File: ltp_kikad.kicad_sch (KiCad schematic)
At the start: 27 parts, among them J2 RPi_GPIO, J3 SM04B-SRSS-TB(LF)(SN)

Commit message: Version 0.05
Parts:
- removed C6 (x2): 4.7uF, Capacitor_SMD:C_0603_1608Metric, symbol Device:C_Small
- removed C7 (x2): 0.1uF, Capacitor_SMD:C_0603_1608Metric, symbol Device:C_Small
- removed J3: SM04B-SRSS-TB(LF)(SN), LTP-305G:JST_SM04B-SRSS-TB(LF)(SN), symbol SM04B-SRSS-TB_LF__SN_:SM04B-SRSS-TB(LF)(SN)
- removed R3 (x2), R5 (x2): DNP, Resistor_SMD:R_0603_1608Metric_Pad0.98x0.95mm_HandSolder, symbol Device:R
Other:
- added sheet Qwiik stemma connector (i2c_connector.kicad_sch)
- note removed: "I2C1_SCL"
- note removed: "I2C1_SDA"
- note removed: "Qwiic/Stemma"
- moved on the sheet: C11

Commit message: Version 0.06
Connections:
- net GND: now also J2.14 (GND), J2.20 (GND), J2.25 (GND), J2.30 (GND), J2.34 (GND), J2.9 (GND)
- no-connect marks 6 -> 5
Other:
- moved on the sheet: C11

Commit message: Add rp2040 mcu, remove mcp2515
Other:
- removed sheet CAN Transiver
- added sheet MCU (mcu.kicad_sch)
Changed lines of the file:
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@@
     (instances
       (project "ltp_kikad"
-        (path "/eed35b77-cbf9-4596-9b17-2558f81058ba/d18f2354-5f56-48bf-919b-3fdf8c87b820"
-          (reference "#PWR045") (unit 1)
-        )
         (path "/eed35b77-cbf9-4596-9b17-2558f81058ba"
           (reference "#PWR058") (unit 1)
@@
     (instances
       (project "ltp_kikad"
-        (path "/eed35b77-cbf9-4596-9b17-2558f81058ba/d18f2354-5f56-48bf-919b-3fdf8c87b820"
-          (reference "#PWR045") (unit 1)
-        )
         (path "/eed35b77-cbf9-4596-9b17-2558f81058ba"
           (reference "#PWR059") (unit 1)
@@
     )
   )
+  (sheet (at 116.84 33.02) (size 57.15 7.62) (fields_autoplaced)
+    (stroke (width 0.1524) (type solid))
+    (fill (color 0 0 0 0.0000))
+    (property "Sheetname" "MCU" (at 116.84 32.3084 0)
+      (effects (font (size 1.27 1.27)) (justify left bottom))
+    )
+    (property "Sheetfile" "mcu.kicad_sch" (at 116.84 41.2246 0)
+      (effects (font (size 1.27 1.27)) (justify left top))
+    )
+    (instances
+      (project "ltp_kikad"
+        (path "/eed35b77-cbf9-4596-9b17-2558f81058ba" (page "6"))
+      )
+    )
+  )
   (sheet (at 116.84 59.69) (size 57.15 7.62) (fields_autoplaced)
     (stroke (width 0.1524) (type solid))
@@
       )
     )
-  )
-  (sheet (at 116.84 45.72) (size 57.15 7.62) (fields_autoplaced)
-    (stroke (width 0.1524) (type solid))
-    (fill (color 0 0 0 0.0000))
-    (property "Sheetname" "CAN Transiver" (at 116.84 45.0084 0)
-      (effects (font (size 1.27 1.27)) (justify left bottom))
-    )
-    (property "Sheetfile" "mdlh_can_ransiver.kicad_sch" (at 116.84 53.9246 0)
-      (effects (font (size 1.27 1.27)) (justify left top))
-    )
-    (instances
-      (project "ltp_kikad"
-        (path "/eed35b77-cbf9-4596-9b17-2558f81058ba" (page "2"))
-      )
-    )

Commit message: Add mcp 2517 can transceiver
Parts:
- removed C11: 10uF, Capacitor_SMD:C_0603_1608Metric, symbol Device:C_Small
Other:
- added sheet CAN (can.kicad_sch)
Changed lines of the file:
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@@
-    (stroke (width 0) (type default))
-  )
-  (wire (pts (xy 242.57 101.6) (xy 242.57 109.22))
     (stroke (width 0) (type default))
   )
@@
         (path "/eed35b77-cbf9-4596-9b17-2558f81058ba"
           (reference "#PWR013") (unit 1)
-        )
-      )
-    )
-  )
-  (symbol (lib_id "power:GND") (at 242.57 114.3 0) (unit 1)
-    (in_bom yes) (on_board yes) (dnp no)
-    (property "Reference" "#PWR038" (at 242.57 120.65 0)
-      (effects (font (size 1.27 1.27)) hide)
-    )
-    (property "Value" "GND" (at 242.697 118.6942 0)
-      (effects (font (size 1.27 1.27)))
-    )
-    (property "Footprint" "" (at 242.57 114.3 0)
-      (effects (font (size 1.27 1.27)) hide)
-    )
-    (property "Datasheet" "" (at 242.57 114.3 0)
-      (effects (font (size 1.27 1.27)) hide)
-    )
-    (pin "1")
-    (instances
-      (project "LTP305_ESP32_CLOCK"
-        (path "/c007e288-8439-49d9-bbdf-49724c34958c"
-          (reference "#PWR038") (unit 1)
-        )
-      )
-      (project "ltp_kikad"
-        (path "/eed35b77-cbf9-4596-9b17-2558f81058ba"
-          (reference "#PWR034") (unit 1)
         )
       )
@@
     )
   )
-  (symbol (lib_id "power:+5V") (at 242.57 101.6 270) (unit 1)
-    (in_bom yes) (on_board yes) (dnp no)
-    (property "Reference" "#PWR08" (at 238.76 101.6 0)
-      (effects (font (size 1.27 1.27)) hide)
-    )
-    (property "Value" "+5V" (at 246.9642 101.981 0)
-      (effects (font (size 1.27 1.27)))
-    )
-    (property "Footprint" "" (at 242.57 101.6 0)
-      (effects (font (size 1.27 1.27)) hide)
-    )
-    (property "Datasheet" "" (at 242.57 101.6 0)
-      (effects (font (size 1.27 1.27)) hide)
-    )
-    (pin "1")
-    (instances
-      (project "LTP305_ESP32_CLOCK"
-        (path "/c007e288-8439-49d9-bbdf-49724c34958c"
-          (reference "#PWR08") (unit 1)
-        )
-      )
-      (project "ltp_kikad"
-        (path "/eed35b77-cbf9-4596-9b17-2558f81058ba"
-          (reference "#PWR033") (unit 1)
-        )
-      )
-    )
-  )
   (symbol (lib_id "LTP-305G:LTP-305G") (at 30.48 92.71 0) (unit 1)
     (in_bom yes) (on_board yes) (dnp no) (fields_autoplaced)
@@
     )
   )
-  (symbol (lib_id "Device:C_Small") (at 242.57 111.76 0) (unit 1)
-    (in_bom yes) (on_board yes) (dnp no)
-    (property "Reference" "C11" (at 244.9068 110.5916 0)
-      (effects (font (size 1.27 1.27)) (justify left))
-    )
-    (property "Value" "10uF" (at 237.49 114.3 0)
-      (effects (font (size 1.27 1.27)) (justify left))
-    )
-    (property "Footprint" "Capacitor_SMD:C_0603_1608Metric" (at 242.57 111.76 0)
-      (effects (font (size 1.27 1.27)) hide)
-    )
-    (property "Datasheet" "~" (at 242.57 111.76 0)
-      (effects (font (size 1.27 1.27)) hide)
-    )
-    (pin "1")
-    (pin "2")
-    (instances
-      (project "LTP305_ESP32_CLOCK"
-        (path "/c007e288-8439-49d9-bbdf-49724c34958c"
-          (reference "C11") (unit 1)
-        )
-      )
-      (project "ltp_kikad"
-        (path "/eed35b77-cbf9-4596-9b17-2558f81058ba"
-          (reference "C17") (unit 1)
-        )
-      )
-    )
-  )
   (symbol (lib_id "Device:C_Small") (at 163.83 114.3 0) (unit 1)
     (in_bom yes) (on_board yes) (dnp no)
@@
           (reference "#PWR025") (unit 1)
         )
+      )
+    )
+  )
+  (sheet (at 116.84 20.32) (size 57.15 6.35) (fields_autoplaced)
+    (stroke (width 0.1524) (type solid))
+    (fill (color 0 0 0 0.0000))
+    (property "Sheetname" "CAN" (at 116.84 19.6084 0)
+      (effects (font (size 1.27 1.27)) (justify left bottom))
+    )
+    (property "Sheetfile" "can.kicad_sch" (at 116.84 27.2546 0)
+      (effects (font (size 1.27 1.27)) (justify left top))
+    )
+    (instances
+      (project "ltp_kikad"
+        (path "/eed35b77-cbf9-4596-9b17-2558f81058ba" (page "6"))
       )
     )
@@
     (instances
       (project "ltp_kikad"
-        (path "/eed35b77-cbf9-4596-9b17-2558f81058ba" (page "6"))
-      )
-    )
+        (path "/eed35b77-cbf9-4596-9b17-2558f81058ba" (page "7"))
+      )
+    )

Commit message: Verssion 0.11
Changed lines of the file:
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@@
   (junction (at 267.97 41.91) (diameter 0) (color 0 0 0 0)
+  )
+  (junction (at 213.36 41.91) (diameter 0) (color 0 0 0 0)
   )
   (no_connect (at 212.09 49.53))
@@
     (stroke (width 0) (type default))
   )
+  (wire (pts (xy 203.2 41.91) (xy 213.36 41.91))
+    (stroke (width 0) (type default))
+  )
   (wire (pts (xy 274.32 58.42) (xy 274.32 57.15))
     (stroke (width 0) (type default))
@@
     (stroke (width 0) (type default))
   )
-  (wire (pts (xy 203.2 41.91) (xy 217.17 41.91))
-    (stroke (width 0) (type default))
-  )
   (wire (pts (xy 267.97 41.91) (xy 271.78 41.91))
     (stroke (width 0) (type default))
@@
     (stroke (width 0) (type default))
   )
+  (wire (pts (xy 213.36 39.37) (xy 213.36 41.91))
+    (stroke (width 0) (type default))
+  )
   (wire (pts (xy 154.94 129.54) (xy 154.94 137.16))
     (stroke (width 0) (type default))
@@
   )
   (wire (pts (xy 91.44 40.64) (xy 97.79 40.64))
+    (stroke (width 0) (type default))
+  )
+  (wire (pts (xy 213.36 41.91) (xy 217.17 41.91))
     (stroke (width 0) (type default))
   )
@@
         )
       )
+    )
+  )
+  (symbol (lib_id "rpi-pico-debugger-shoe-rescue:+3.3V-power") (at 213.36 39.37 0) (unit 1)
+    (in_bom yes) (on_board yes) (dnp no)
+    (property "Reference" "#PWR0104" (at 213.36 43.18 0)
+      (effects (font (size 1.27 1.27)) hide)
+    )
+    (property "Value" "+3.3V" (at 213.741 34.9758 0)
+      (effects (font (size 1.27 1.27)))
+    )
+    (property "Footprint" "" (at 213.36 39.37 0)
+      (effects (font (size 1.27 1.27)) hide)
+    )
+    (property "Datasheet" "" (at 213.36 39.37 0)
+      (effects (font (size 1.27 1.27)) hide)
+    )
+    (pin "1")
+    (instances
+      (project "rpi-pico-debugger-shoe"
+        (path "/aad74d97-f116-4a83-b498-c8cb2f4b4e35"
+          (reference "#PWR0104") (unit 1)
+        )
+      )
+      (project "ltp_kikad"
+        (path "/eed35b77-cbf9-4596-9b17-2558f81058ba/643f5372-7b7f-4a0a-9eb8-fe959bdc465c"
+          (reference "#PWR056") (unit 1)
+        )
+        (path "/eed35b77-cbf9-4596-9b17-2558f81058ba/016e13d7-1a1a-4980-89bb-e5d4ebfcb8b8"
+          (reference "#PWR0117") (unit 1)
+        )
+        (path "/eed35b77-cbf9-4596-9b17-2558f81058ba"
+          (reference "#PWR0119") (unit 1)
+        )
+      )

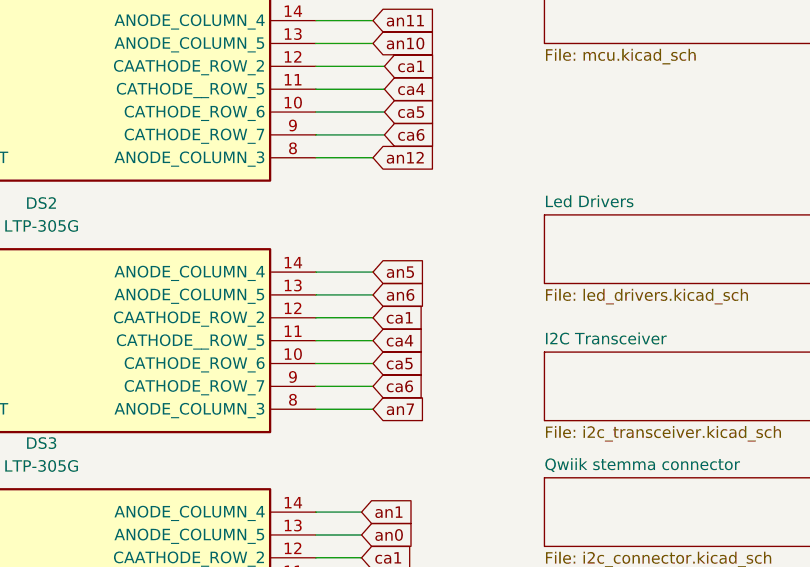
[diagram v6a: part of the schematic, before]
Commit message: Fix connection on an6 an5 ds2
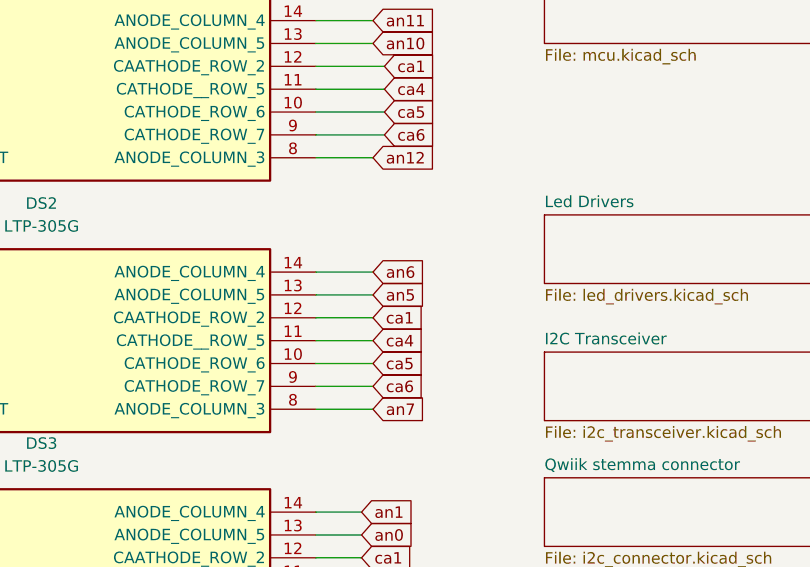
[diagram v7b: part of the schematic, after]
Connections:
- net an5: now also DS2.13 (ANODE_COLUMN_5); no longer DS2.14 (ANODE_COLUMN_4)
- net an6: now also DS2.14 (ANODE_COLUMN_4); no longer DS2.13 (ANODE_COLUMN_5)
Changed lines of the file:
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@@
     )
   )
-  (global_label "an6" (shape input) (at 97.79 68.58 0) (fields_autoplaced)
+  (global_label "ca2" (shape input) (at 25.4 71.12 180) (fields_autoplaced)
+    (effects (font (size 1.27 1.27)) (justify right))
+    (property "Intersheetrefs" "${INTERSHEET_REFS}" (at 19.0471 71.12 0)
+      (effects (font (size 1.27 1.27)) (justify right) hide)
+    )
+  )
+  (global_label "an14" (shape input) (at 25.4 48.26 180) (fields_autoplaced)
+    (effects (font (size 1.27 1.27)) (justify right))
+    (property "Intersheetrefs" "${INTERSHEET_REFS}" (at 17.7772 48.26 0)
+      (effects (font (size 1.27 1.27)) (justify right) hide)
+    )
+  )
+  (global_label "ca4" (shape input) (at 99.06 45.72 0) (fields_autoplaced)
+    (effects (font (size 1.27 1.27)) (justify left))
+    (property "Intersheetrefs" "${INTERSHEET_REFS}" (at 105.4129 45.72 0)
+      (effects (font (size 1.27 1.27)) (justify left) hide)
+    )
+  )
+  (global_label "2_ca2" (shape input) (at 24.13 175.26 180)
+    (effects (font (size 1.27 1.27)) (justify right))
+    (property "Intersheetrefs" "${INTERSHEET_REFS}" (at 24.13 175.26 0)
+      (effects (font (size 1.27 1.27)) hide)
+    )
+  )
+  (global_label "an10" (shape input) (at 97.79 40.64 0) (fields_autoplaced)
+    (effects (font (size 1.27 1.27)) (justify left))
+    (property "Intersheetrefs" "${INTERSHEET_REFS}" (at 105.4128 40.64 0)
+      (effects (font (size 1.27 1.27)) (justify left) hide)
+    )
+  )
+  (global_label "2_an3" (shape input) (at 24.13 170.18 180)
+    (effects (font (size 1.27 1.27)) (justify right))
+    (property "Intersheetrefs" "${INTERSHEET_REFS}" (at 24.13 170.18 0)
+      (effects (font (size 1.27 1.27)) hide)
+    )
+  )
+  (global_label "3.3_SCL" (shape input) (at 198.12 46.99 180)
+    (effects (font (size 1.27 1.27)) (justify right))
+    (property "Intersheetrefs" "${INTERSHEET_REFS}" (at 191.7066 46.99 0)
+      (effects (font (size 1.27 1.27)) hide)
+    )
+  )
+  (global_label "an6" (shape input) (at 97.79 66.04 0) (fields_autoplaced)
+    (effects (font (size 1.27 1.27)) (justify left))
+    (property "Intersheetrefs" "${INTERSHEET_REFS}" (at 104.2033 66.04 0)
+      (effects (font (size 1.27 1.27)) (justify left) hide)
+    )
+  )
+  (global_label "ca2" (shape input) (at 24.13 97.79 180) (fields_autoplaced)
+    (effects (font (size 1.27 1.27)) (justify right))
+    (property "Intersheetrefs" "${INTERSHEET_REFS}" (at 17.7771 97.79 0)
+      (effects (font (size 1.27 1.27)) (justify right) hide)
+    )
+  )
+  (global_label "2_an13" (shape input) (at 25.4 118.11 180)
+    (effects (font (size 1.27 1.27)) (justify right))
+    (property "Intersheetrefs" "${INTERSHEET_REFS}" (at 25.4 118.11 0)
+      (effects (font (size 1.27 1.27)) hide)
+    )
+  )
+  (global_label "2_ca0" (shape input) (at 24.13 172.72 180)
+    (effects (font (size 1.27 1.27)) (justify right))
+    (property "Intersheetrefs" "${INTERSHEET_REFS}" (at 24.13 172.72 0)
+      (effects (font (size 1.27 1.27)) hide)
+    )
+  )
+  (global_label "an4" (shape input) (at 24.13 102.87 180) (fields_autoplaced)
+    (effects (font (size 1.27 1.27)) (justify right))
+    (property "Intersheetrefs" "${INTERSHEET_REFS}" (at 17.7167 102.87 0)
+      (effects (font (size 1.27 1.27)) (justify right) hide)
+    )
+  )
+  (global_label "2_an12" (shape input) (at 97.79 133.35 0)
+    (effects (font (size 1.27 1.27)) (justify left))
+    (property "Intersheetrefs" "${INTERSHEET_REFS}" (at 97.79 133.35 0)
+      (effects (font (size 1.27 1.27)) hide)
+    )
+  )
+  (global_label "2_ca4" (shape input) (at 97.79 125.73 0)
+    (effects (font (size 1.27 1.27)) (justify left))
+    (property "Intersheetrefs" "${INTERSHEET_REFS}" (at 97.79 125.73 0)
+      (effects (font (size 1.27 1.27)) hide)
+    )
+  )
+  (global_label "2_ca0" (shape input) (at 25.4 120.65 180)
+    (effects (font (size 1.27 1.27)) (justify right))
+    (property "Intersheetrefs" "${INTERSHEET_REFS}" (at 25.4 120.65 0)
+      (effects (font (size 1.27 1.27)) hide)
+    )
+  )
+  (global_label "ca5" (shape input) (at 99.06 48.26 0) (fields_autoplaced)
+    (effects (font (size 1.27 1.27)) (justify left))
+    (property "Intersheetrefs" "${INTERSHEET_REFS}" (at 105.4129 48.26 0)
+      (effects (font (size 1.27 1.27)) (justify left) hide)
+    )
+  )
+  (global_label "3.3_SDA" (shape input) (at 198.12 44.45 180)
+    (effects (font (size 1.27 1.27)) (justify right))
+    (property "Intersheetrefs" "${INTERSHEET_REFS}" (at 198.12 44.45 0)
+      (effects (font (size 1.27 1.27)) hide)
+    )
+  )
+  (global_label "an5" (shape input) (at 97.79 68.58 0) (fields_autoplaced)
     (effects (font (size 1.27 1.27)) (justify left))
     (property "Intersheetrefs" "${INTERSHEET_REFS}" (at 104.2033 68.58 0)
@@
     )
   )
-  (global_label "ca2" (shape input) (at 25.4 71.12 180) (fields_autoplaced)
-    (effects (font (size 1.27 1.27)) (justify right))
-    (property "Intersheetrefs" "${INTERSHEET_REFS}" (at 19.0471 71.12 0)
-      (effects (font (size 1.27 1.27)) (justify right) hide)
-    )
-  )
-  (global_label "an14" (shape input) (at 25.4 48.26 180) (fields_autoplaced)
-    (effects (font (size 1.27 1.27)) (justify right))
-    (property "Intersheetrefs" "${INTERSHEET_REFS}" (at 17.7772 48.26 0)
-      (effects (font (size 1.27 1.27)) (justify right) hide)
-    )
-  )
-  (global_label "ca4" (shape input) (at 99.06 45.72 0) (fields_autoplaced)
-    (effects (font (size 1.27 1.27)) (justify left))
-    (property "Intersheetrefs" "${INTERSHEET_REFS}" (at 105.4129 45.72 0)
-      (effects (font (size 1.27 1.27)) (justify left) hide)
-    )
-  )
-  (global_label "2_ca2" (shape input) (at 24.13 175.26 180)
-    (effects (font (size 1.27 1.27)) (justify right))
-    (property "Intersheetrefs" "${INTERSHEET_REFS}" (at 24.13 175.26 0)
-      (effects (font (size 1.27 1.27)) hide)
-    )
-  )
-  (global_label "an10" (shape input) (at 97.79 40.64 0) (fields_autoplaced)
-    (effects (font (size 1.27 1.27)) (justify left))
-    (property "Intersheetrefs" "${INTERSHEET_REFS}" (at 105.4128 40.64 0)
-      (effects (font (size 1.27 1.27)) (justify left) hide)
-    )
-  )
-  (global_label "2_an3" (shape input) (at 24.13 170.18 180)
-    (effects (font (size 1.27 1.27)) (justify right))
-    (property "Intersheetrefs" "${INTERSHEET_REFS}" (at 24.13 170.18 0)
-      (effects (font (size 1.27 1.27)) hide)
-    )
-  )
-  (global_label "3.3_SCL" (shape input) (at 198.12 46.99 180)
-    (effects (font (size 1.27 1.27)) (justify right))
-    (property "Intersheetrefs" "${INTERSHEET_REFS}" (at 191.7066 46.99 0)
-      (effects (font (size 1.27 1.27)) hide)
-    )
-  )
-  (global_label "ca2" (shape input) (at 24.13 97.79 180) (fields_autoplaced)
-    (effects (font (size 1.27 1.27)) (justify right))
-    (property "Intersheetrefs" "${INTERSHEET_REFS}" (at 17.7771 97.79 0)
-      (effects (font (size 1.27 1.27)) (justify right) hide)
-    )
-  )
-  (global_label "2_an13" (shape input) (at 25.4 118.11 180)
-    (effects (font (size 1.27 1.27)) (justify right))
-    (property "Intersheetrefs" "${INTERSHEET_REFS}" (at 25.4 118.11 0)
-      (effects (font (size 1.27 1.27)) hide)
-    )
-  )
-  (global_label "2_ca0" (shape input) (at 24.13 172.72 180)
-    (effects (font (size 1.27 1.27)) (justify right))
-    (property "Intersheetrefs" "${INTERSHEET_REFS}" (at 24.13 172.72 0)
-      (effects (font (size 1.27 1.27)) hide)
-    )
-  )
-  (global_label "an4" (shape input) (at 24.13 102.87 180) (fields_autoplaced)
-    (effects (font (size 1.27 1.27)) (justify right))
-    (property "Intersheetrefs" "${INTERSHEET_REFS}" (at 17.7167 102.87 0)
-      (effects (font (size 1.27 1.27)) (justify right) hide)
-    )
-  )
-  (global_label "2_an12" (shape input) (at 97.79 133.35 0)
-    (effects (font (size 1.27 1.27)) (justify left))
-    (property "Intersheetrefs" "${INTERSHEET_REFS}" (at 97.79 133.35 0)
-      (effects (font (size 1.27 1.27)) hide)
-    )
-  )
-  (global_label "2_ca4" (shape input) (at 97.79 125.73 0)
-    (effects (font (size 1.27 1.27)) (justify left))
-    (property "Intersheetrefs" "${INTERSHEET_REFS}" (at 97.79 125.73 0)
-      (effects (font (size 1.27 1.27)) hide)
-    )
-  )
-  (global_label "2_ca0" (shape input) (at 25.4 120.65 180)
-    (effects (font (size 1.27 1.27)) (justify right))
-    (property "Intersheetrefs" "${INTERSHEET_REFS}" (at 25.4 120.65 0)
-      (effects (font (size 1.27 1.27)) hide)
-    )
-  )
-  (global_label "ca5" (shape input) (at 99.06 48.26 0) (fields_autoplaced)
-    (effects (font (size 1.27 1.27)) (justify left))
-    (property "Intersheetrefs" "${INTERSHEET_REFS}" (at 105.4129 48.26 0)
-      (effects (font (size 1.27 1.27)) (justify left) hide)
-    )
-  )
-  (global_label "3.3_SDA" (shape input) (at 198.12 44.45 180)
-    (effects (font (size 1.27 1.27)) (justify right))
-    (property "Intersheetrefs" "${INTERSHEET_REFS}" (at 198.12 44.45 0)
-      (effects (font (size 1.27 1.27)) hide)
-    )
-  )
   (global_label "ca6" (shape input) (at 96.52 105.41 0) (fields_autoplaced)
     (effects (font (size 1.27 1.27)) (justify left))
@@
     )
   )
-  (global_label "an5" (shape input) (at 97.79 66.04 0) (fields_autoplaced)
-    (effects (font (size 1.27 1.27)) (justify left))
-    (property "Intersheetrefs" "${INTERSHEET_REFS}" (at 104.2033 66.04 0)
-      (effects (font (size 1.27 1.27)) (justify left) hide)
-    )
-  )

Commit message: Simplify design
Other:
- removed sheet CAN
- removed sheet MCU
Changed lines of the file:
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@@
       )
       (project "ltp_kikad"
-        (path "/eed35b77-cbf9-4596-9b17-2558f81058ba/643f5372-7b7f-4a0a-9eb8-fe959bdc465c"
-          (reference "#PWR056") (unit 1)
-        )
-        (path "/eed35b77-cbf9-4596-9b17-2558f81058ba/016e13d7-1a1a-4980-89bb-e5d4ebfcb8b8"
-          (reference "#PWR0117") (unit 1)
-        )
         (path "/eed35b77-cbf9-4596-9b17-2558f81058ba"
           (reference "#PWR0119") (unit 1)
@@
     )
   )
-  (sheet (at 116.84 20.32) (size 57.15 6.35) (fields_autoplaced)
-    (stroke (width 0.1524) (type solid))
-    (fill (color 0 0 0 0.0000))
-    (property "Sheetname" "CAN" (at 116.84 19.6084 0)
-      (effects (font (size 1.27 1.27)) (justify left bottom))
-    )
-    (property "Sheetfile" "can.kicad_sch" (at 116.84 27.2546 0)
-      (effects (font (size 1.27 1.27)) (justify left top))
-    )
-    (instances
-      (project "ltp_kikad"
-        (path "/eed35b77-cbf9-4596-9b17-2558f81058ba" (page "6"))
-      )
-    )
-  )
   (sheet (at 116.84 74.93) (size 57.15 7.62) (fields_autoplaced)
     (stroke (width 0.1524) (type solid))
@@
       )
     )
-  )
-  (sheet (at 116.84 33.02) (size 57.15 7.62) (fields_autoplaced)
-    (stroke (width 0.1524) (type solid))
-    (fill (color 0 0 0 0.0000))
-    (property "Sheetname" "MCU" (at 116.84 32.3084 0)
-      (effects (font (size 1.27 1.27)) (justify left bottom))
-    )
-    (property "Sheetfile" "mcu.kicad_sch" (at 116.84 41.2246 0)
-      (effects (font (size 1.27 1.27)) (justify left top))
-    )
-    (instances
-      (project "ltp_kikad"
-        (path "/eed35b77-cbf9-4596-9b17-2558f81058ba" (page "7"))
-      )
-    )
